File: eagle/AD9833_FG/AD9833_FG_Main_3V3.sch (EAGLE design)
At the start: 12 parts, among them IC1 AD822N

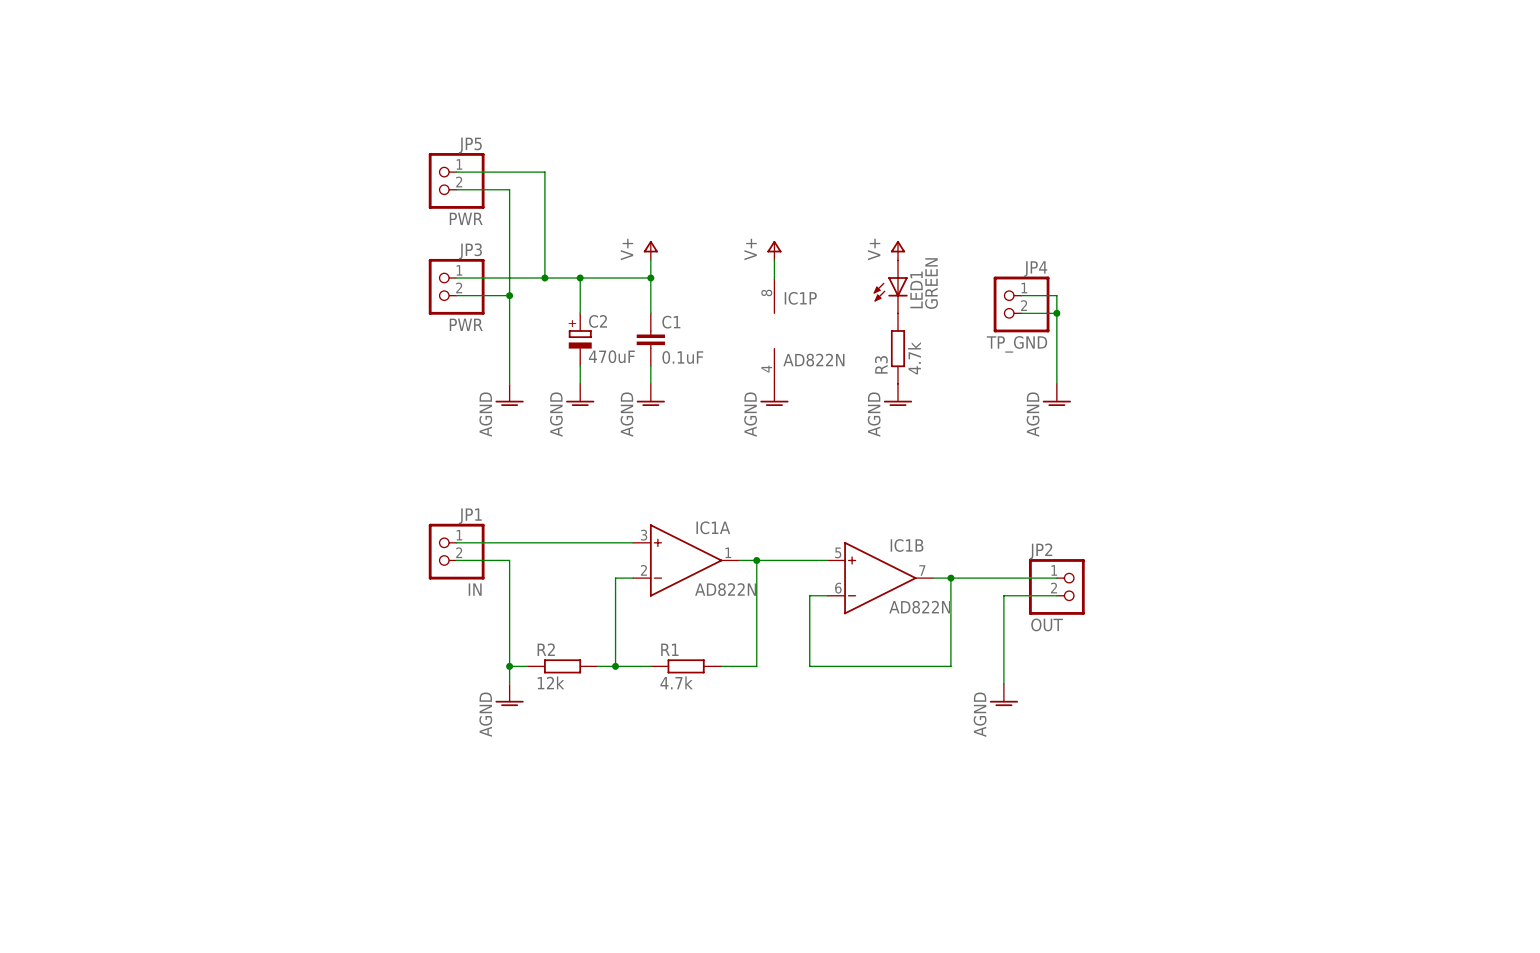
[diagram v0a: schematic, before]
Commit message: 3.3V Version
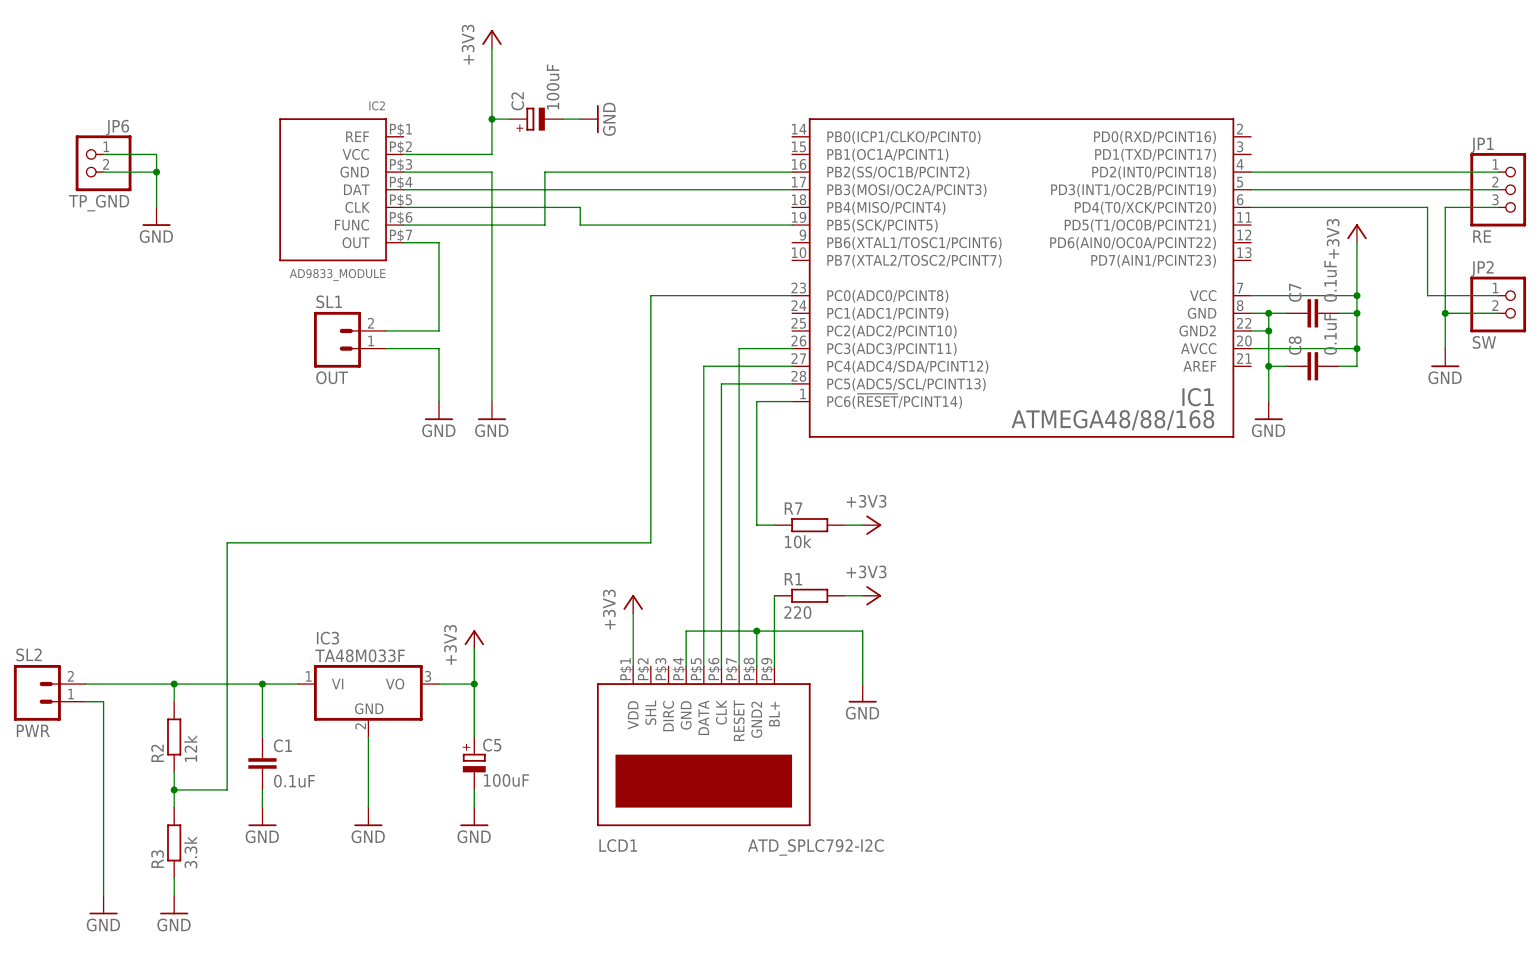
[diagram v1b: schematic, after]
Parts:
- removed JP3, JP5: PWR, pinhead:PINHD-1X2
- removed JP4: TP_GND, pinhead:PINHD-1X2
- removed LED1: GREEN, led:LED3MM
- added C5: 100uF, rcl:CPOL-EUSANYO_C
- added C7, C8: 0.1uF, rcl:C-EU025-024X044
- added IC2: AD9833_MODULE, mylib2:AD9833_MODULE
- added IC3: TA48M033F, mylib2:TA48M033F
- added JP6: TP_GND, pinhead:PINHD-1X2
- added LCD1: ATD_SPLC792-I2C, mylib2:ATD_SPLC792-I2C
- added R7: 10k, rcl:R-EU_0207/7
- added SL1: OUT, con-amp-quick:M02
- added SL2: PWR, con-amp-quick:M02
- C2: value 470uF -> 100uF; device rcl:CPOL-EUE2.5-7 -> rcl:CPOL-EUSANYO_C
- IC1: value AD822N -> ATMEGA48/88/168; device analog-devices:AD822N -> mylib2:ATMEGA48/88/168
- JP1: value IN -> RE; device pinhead:PINHD-1X2 -> pinhead:PINHD-1X3
- JP2: value OUT -> SW
- R1: value 4.7k -> 220
- R3: value 4.7k -> 3.3k
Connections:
- removed net AGND: C1.2, C2.-, IC1P.V-, JP1.2, JP2.2, JP3.2, JP4.1, JP4.2, JP5.2, R2.1, R3.1
- removed net V+: C1.1, C2.+, IC1P.V+, JP3.1, JP5.1, LED1.A
- new net +3V3: C2.+, C5.+, C7.2, C8.2, IC1.AVCC, IC1.VCC, IC2.VCC, IC3.VO, LCD1.VDD, R1.2, R7.2
- new net GND: C1.2, C2.-, C5.-, C7.1, C8.1, IC1.GND, IC1.GND2, IC2.GND, IC3.GND, JP1.3, JP2.2, JP6.1, JP6.2, LCD1.GND, LCD1.GND2, R3.1, SL1.1, SL2.1
- new net N$10: IC1.PD4(T0/XCK/PCINT20), JP2.1
- new net N$14: LCD1.BL+, R1.1
- new net N$15: C1.1, IC3.VI, R2.2, SL2.2
- new net N$16: IC1.PC0(ADC0/PCINT8), R2.1, R3.2
- new net N$18: IC1.PC6(!RESET!/PCINT14), R7.1
- new net N$2: IC1.PB5(SCK/PCINT5), IC2.CLK
- new net N$6: IC2.OUT, SL1.2
- new net N$7: IC1.PC3(ADC3/PCINT11), LCD1.RESET
- new net N$9: IC1.PD3(INT1/OC2B/PCINT19), JP1.2
- net N$1: now also IC1.PB3(MOSI/OC2A/PCINT3), IC2.DAT; no longer IC1A.IN-, R1.1, R2.2
- net N$3: now also IC1.PB2(SS/OC1B/PCINT2), IC2.FUNC; no longer IC1A.IN+, JP1.1
- net N$4: now also IC1.PC5(ADC5/SCL/PCINT13), LCD1.CLK; no longer IC1A.OUT, IC1B.IN+, R1.2
- net N$5: now also IC1.PC4(ADC4/SDA/PCINT12), LCD1.DATA; no longer IC1B.IN-, IC1B.OUT, JP2.1
- net N$8: now also IC1.PD2(INT0/PCINT18), JP1.1; no longer LED1.C, R3.2
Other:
- moved on the sheet: C1, C2, JP2, R1, R2, R3

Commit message: Board Design
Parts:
- added SL3: PWR, con-amp-quick:M02
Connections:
- net GND: now also SL2.2, SL3.1; no longer SL2.1
- net N$15: now also SL2.1, SL3.2; no longer SL2.2
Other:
- moved on the sheet: SL2
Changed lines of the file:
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@@
 <setting verticaltext="up"/>
 </settings>
-<grid distance="0.1" unitdist="inch" unit="inch" style="lines" multiple="1" display="yes" altdistance="0.01" altunitdist="inch" altunit="inch"/>
+<grid distance="0.1" unitdist="inch" unit="inch" style="lines" multiple="1" display="no" altdistance="0.01" altunitdist="inch" altunit="inch"/>
 <layers>
 <layer number="1" name="Top" color="4" fill="1" visible="no" active="no"/>
@@
 <part name="C2" library="rcl" deviceset="CPOL-EU" device="SANYO_C" value="100uF"/>
 <part name="GND4" library="supply1" deviceset="GND" device=""/>
+<part name="SL3" library="con-amp-quick" deviceset="M02" device="" value="PWR"/>
 </parts>
 <sheets>
@@
 <instance part="C8" gate="G$1" x="210.82" y="111.76" rot="R90"/>
 <instance part="SL1" gate="G$1" x="71.12" y="114.3"/>
-<instance part="SL2" gate="G$1" x="27.94" y="63.5"/>
+<instance part="SL2" gate="G$1" x="27.94" y="66.04" rot="MR180"/>
 <instance part="+3V2" gate="G$1" x="91.44" y="73.66"/>
 <instance part="+3V4" gate="G$1" x="93.98" y="160.02"/>
@@
 <instance part="C2" gate="G$1" x="99.06" y="147.32" rot="R90"/>
 <instance part="GND4" gate="1" x="109.22" y="147.32" rot="R90"/>
+<instance part="SL3" gate="G$1" x="27.94" y="48.26"/>
 </instances>
 <busses>
@@
 <segment>
 <pinref part="GND3" gate="1" pin="GND"/>
+<pinref part="JP1" gate="A" pin="3"/>
 <wire x1="231.14" y1="114.3" x2="231.14" y2="119.38" width="0.1524" layer="91"/>
-<pinref part="JP1" gate="A" pin="3"/>
 <wire x1="231.14" y1="119.38" x2="231.14" y2="134.62" width="0.1524" layer="91"/>
 <wire x1="231.14" y1="134.62" x2="238.76" y2="134.62" width="0.1524" layer="91"/>
@@
 </segment>
 <segment>
+<pinref part="GND7" gate="1" pin="GND"/>
+<wire x1="38.1" y1="63.5" x2="38.1" y2="48.26" width="0.1524" layer="91"/>
+<pinref part="SL3" gate="G$1" pin="1"/>
+<wire x1="38.1" y1="48.26" x2="38.1" y2="35.56" width="0.1524" layer="91"/>
+<wire x1="35.56" y1="48.26" x2="38.1" y2="48.26" width="0.1524" layer="91"/>
+<junction x="38.1" y="48.26"/>
+<pinref part="SL2" gate="G$1" pin="2"/>
 <wire x1="35.56" y1="63.5" x2="38.1" y2="63.5" width="0.1524" layer="91"/>
-<pinref part="GND7" gate="1" pin="GND"/>
-<wire x1="38.1" y1="63.5" x2="38.1" y2="35.56" width="0.1524" layer="91"/>
-<pinref part="SL2" gate="G$1" pin="1"/>
 </segment>
 <segment>
@@
 <net name="N$15" class="0">
 <segment>
-<wire x1="35.56" y1="66.04" x2="48.26" y2="66.04" width="0.1524" layer="91"/>
+<wire x1="43.18" y1="66.04" x2="48.26" y2="66.04" width="0.1524" layer="91"/>
 <wire x1="48.26" y1="66.04" x2="60.96" y2="66.04" width="0.1524" layer="91"/>
 <wire x1="60.96" y1="58.42" x2="60.96" y2="66.04" width="0.1524" layer="91"/>
@@
 <wire x1="48.26" y1="63.5" x2="48.26" y2="66.04" width="0.1524" layer="91"/>
 <junction x="48.26" y="66.04"/>
-<pinref part="SL2" gate="G$1" pin="2"/>
 <wire x1="66.04" y1="66.04" x2="60.96" y2="66.04" width="0.1524" layer="91"/>
 <junction x="60.96" y="66.04"/>
 <pinref part="C1" gate="G$1" pin="1"/>
 <pinref part="IC3" gate="G$1" pin="VI"/>
-</segment>
-</net>
+<pinref part="SL3" gate="G$1" pin="2"/>
+<wire x1="35.56" y1="50.8" x2="43.18" y2="50.8" width="0.1524" layer="91"/>
+<wire x1="43.18" y1="50.8" x2="43.18" y2="66.04" width="0.1524" layer="91"/>
+<pinref part="SL2" gate="G$1" pin="1"/>
+<wire x1="35.56" y1="66.04" x2="43.18" y2="66.04" width="0.1524" layer="91"/>
+<junction x="43.18" y="66.04"/>
+</segment>
+</net>

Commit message: Update eagle files
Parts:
- removed R3: 3.3k, rcl:R-EU_0207/7
- removed SL3: PWR, con-amp-quick:M02
- added JP3: TP_3V3, pinhead:PINHD-1X2
- added R4: 100k, pot:TRIM_EU-B25P
- C5: device rcl:CPOL-EUSANYO_C -> rcl:CPOL-EUE2.5-7
- C8: device rcl:C-EU025-024X044 -> rcl:C-EU050-024X044
- R2: value 12k -> 220k
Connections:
- new net N$11: R2.1, R4.E
- net +3V3: now also JP3.1, JP3.2
- net GND: now also R4.A; no longer R3.1, SL3.1
- net N$15: no longer SL3.2
- net N$16: now also R4.S; no longer R2.1, R3.2
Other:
- moved on the sheet: JP6
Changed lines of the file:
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@@
 <setting verticaltext="up"/>
 </settings>
-<grid distance="0.1" unitdist="inch" unit="inch" style="lines" multiple="1" display="no" altdistance="0.01" altunitdist="inch" altunit="inch"/>
+<grid distance="0.1" unitdist="inch" unit="inch" style="lines" multiple="1" display="yes" altdistance="0.01" altunitdist="inch" altunit="inch"/>
 <layers>
 <layer number="1" name="Top" color="4" fill="1" visible="no" active="no"/>
@@
 <part name="GND8" library="supply1" deviceset="GND" device=""/>
 <part name="GND9" library="supply1" deviceset="GND" device=""/>
-<part name="C5" library="rcl" deviceset="CPOL-EU" device="SANYO_C" value="100uF"/>
+<part name="C5" library="rcl" deviceset="CPOL-EU" device="E2.5-7" value="100uF"/>
 <part name="GND11" library="supply1" deviceset="GND" device=""/>
-<part name="R2" library="rcl" deviceset="R-EU_" device="0207/7" value="12k"/>
-<part name="R3" library="rcl" deviceset="R-EU_" device="0207/7" value="3.3k"/>
+<part name="R2" library="rcl" deviceset="R-EU_" device="0207/7" value="220k"/>
 <part name="GND12" library="supply1" deviceset="GND" device=""/>
 <part name="FRAME1" library="frames" deviceset="A4L-LOC" device="" value="Frame"/>
@@
 <part name="GND18" library="supply1" deviceset="GND" device=""/>
 <part name="C7" library="rcl" deviceset="C-EU" device="025-024X044" value="0.1uF"/>
-<part name="C8" library="rcl" deviceset="C-EU" device="025-024X044" value="0.1uF"/>
+<part name="C8" library="rcl" deviceset="C-EU" device="050-024X044" value="0.1uF"/>
 <part name="SL1" library="con-amp-quick" deviceset="M02" device="" value="OUT"/>
 <part name="SL2" library="con-amp-quick" deviceset="M02" device="" value="PWR"/>
@@
 <part name="C2" library="rcl" deviceset="CPOL-EU" device="SANYO_C" value="100uF"/>
 <part name="GND4" library="supply1" deviceset="GND" device=""/>
-<part name="SL3" library="con-amp-quick" deviceset="M02" device="" value="PWR"/>
+<part name="R4" library="pot" deviceset="TRIM_EU-" device="B25P" value="100k"/>
+<part name="JP3" library="pinhead" deviceset="PINHD-1X2" device="" value="TP_3V3"/>
+<part name="+3V3" library="supply1" deviceset="+3V3" device=""/>
 </parts>
 <sheets>
@@
 <instance part="GND11" gate="1" x="91.44" y="45.72"/>
 <instance part="R2" gate="G$1" x="48.26" y="58.42" rot="R90"/>
-<instance part="R3" gate="G$1" x="48.26" y="43.18" rot="R90"/>
 <instance part="GND12" gate="1" x="48.26" y="33.02"/>
 <instance part="FRAME1" gate="G$1" x="0" y="0"/>
-<instance part="JP6" gate="G$1" x="35.56" y="139.7" rot="MR0"/>
-<instance part="GND16" gate="1" x="45.72" y="132.08"/>
+<instance part="JP6" gate="G$1" x="35.56" y="124.46" rot="MR0"/>
+<instance part="GND16" gate="1" x="45.72" y="116.84"/>
 <instance part="R7" gate="G$1" x="139.7" y="88.9"/>
 <instance part="GND18" gate="1" x="205.74" y="104.14"/>
@@
 <instance part="C2" gate="G$1" x="99.06" y="147.32" rot="R90"/>
 <instance part="GND4" gate="1" x="109.22" y="147.32" rot="R90"/>
-<instance part="SL3" gate="G$1" x="27.94" y="48.26"/>
+<instance part="R4" gate="1" x="48.26" y="45.72" smashed="yes">
+<attribute name="NAME" x="42.291" y="41.91" size="1.778" layer="95" rot="R90"/>
+<attribute name="VALUE" x="44.45" y="41.91" size="1.778" layer="96" rot="R90"/>
+</instance>
+<instance part="JP3" gate="G$1" x="35.56" y="142.24" rot="MR0"/>
+<instance part="+3V3" gate="G$1" x="45.72" y="154.94"/>
 </instances>
 <busses>
@@
 <segment>
 <pinref part="GND7" gate="1" pin="GND"/>
-<wire x1="38.1" y1="63.5" x2="38.1" y2="48.26" width="0.1524" layer="91"/>
-<pinref part="SL3" gate="G$1" pin="1"/>
-<wire x1="38.1" y1="48.26" x2="38.1" y2="35.56" width="0.1524" layer="91"/>
-<wire x1="35.56" y1="48.26" x2="38.1" y2="48.26" width="0.1524" layer="91"/>
-<junction x="38.1" y="48.26"/>
+<wire x1="38.1" y1="63.5" x2="38.1" y2="35.56" width="0.1524" layer="91"/>
 <pinref part="SL2" gate="G$1" pin="2"/>
 <wire x1="35.56" y1="63.5" x2="38.1" y2="63.5" width="0.1524" layer="91"/>
@@
 <segment>
 <pinref part="GND12" gate="1" pin="GND"/>
-<pinref part="R3" gate="G$1" pin="1"/>
-<wire x1="48.26" y1="35.56" x2="48.26" y2="38.1" width="0.1524" layer="91"/>
+<wire x1="48.26" y1="35.56" x2="48.26" y2="40.64" width="0.1524" layer="91"/>
+<pinref part="R4" gate="1" pin="A"/>
 </segment>
 <segment>
 <pinref part="JP6" gate="G$1" pin="2"/>
-<wire x1="38.1" y1="139.7" x2="45.72" y2="139.7" width="0.1524" layer="91"/>
-<wire x1="45.72" y1="139.7" x2="45.72" y2="142.24" width="0.1524" layer="91"/>
+<wire x1="38.1" y1="124.46" x2="45.72" y2="124.46" width="0.1524" layer="91"/>
+<wire x1="45.72" y1="124.46" x2="45.72" y2="127" width="0.1524" layer="91"/>
 <pinref part="JP6" gate="G$1" pin="1"/>
-<wire x1="45.72" y1="142.24" x2="38.1" y2="142.24" width="0.1524" layer="91"/>
+<wire x1="45.72" y1="127" x2="38.1" y2="127" width="0.1524" layer="91"/>
 <pinref part="GND16" gate="1" pin="GND"/>
-<wire x1="45.72" y1="139.7" x2="45.72" y2="134.62" width="0.1524" layer="91"/>
-<junction x="45.72" y="139.7"/>
+<wire x1="45.72" y1="124.46" x2="45.72" y2="119.38" width="0.1524" layer="91"/>
+<junction x="45.72" y="124.46"/>
 </segment>
 <segment>
@@
 <pinref part="+3V7" gate="G$1" pin="+3V3"/>
 </segment>
+<segment>
+<pinref part="JP3" gate="G$1" pin="2"/>
+<wire x1="38.1" y1="142.24" x2="45.72" y2="142.24" width="0.1524" layer="91"/>
+<wire x1="45.72" y1="142.24" x2="45.72" y2="144.78" width="0.1524" layer="91"/>
+<pinref part="+3V3" gate="G$1" pin="+3V3"/>
+<pinref part="JP3" gate="G$1" pin="1"/>
+<wire x1="45.72" y1="144.78" x2="45.72" y2="152.4" width="0.1524" layer="91"/>
+<wire x1="38.1" y1="144.78" x2="45.72" y2="144.78" width="0.1524" layer="91"/>
+<junction x="45.72" y="144.78"/>
+</segment>
 </net>
 <net name="N$14" class="0">
@@
 <net name="N$15" class="0">
 <segment>
-<wire x1="43.18" y1="66.04" x2="48.26" y2="66.04" width="0.1524" layer="91"/>
 <wire x1="48.26" y1="66.04" x2="60.96" y2="66.04" width="0.1524" layer="91"/>
 <wire x1="60.96" y1="58.42" x2="60.96" y2="66.04" width="0.1524" layer="91"/>
@@
 <pinref part="C1" gate="G$1" pin="1"/>
 <pinref part="IC3" gate="G$1" pin="VI"/>
-<pinref part="SL3" gate="G$1" pin="2"/>
-<wire x1="35.56" y1="50.8" x2="43.18" y2="50.8" width="0.1524" layer="91"/>
-<wire x1="43.18" y1="50.8" x2="43.18" y2="66.04" width="0.1524" layer="91"/>
 <pinref part="SL2" gate="G$1" pin="1"/>
-<wire x1="35.56" y1="66.04" x2="43.18" y2="66.04" width="0.1524" layer="91"/>
-<junction x="43.18" y="66.04"/>
+<wire x1="35.56" y1="66.04" x2="48.26" y2="66.04" width="0.1524" layer="91"/>
 </segment>
 </net>
@@
 <wire x1="116.84" y1="121.92" x2="137.16" y2="121.92" width="0.1524" layer="91"/>
 <wire x1="116.84" y1="121.92" x2="116.84" y2="86.36" width="0.1524" layer="91"/>
-<wire x1="55.88" y1="50.8" x2="55.88" y2="86.36" width="0.1524" layer="91"/>
+<wire x1="55.88" y1="45.72" x2="55.88" y2="86.36" width="0.1524" layer="91"/>
 <wire x1="116.84" y1="86.36" x2="55.88" y2="86.36" width="0.1524" layer="91"/>
-<pinref part="R2" gate="G$1" pin="1"/>
-<pinref part="R3" gate="G$1" pin="2"/>
-<wire x1="48.26" y1="48.26" x2="48.26" y2="50.8" width="0.1524" layer="91"/>
-<wire x1="48.26" y1="50.8" x2="48.26" y2="53.34" width="0.1524" layer="91"/>
-<wire x1="55.88" y1="50.8" x2="48.26" y2="50.8" width="0.1524" layer="91"/>
-<junction x="48.26" y="50.8"/>
+<pinref part="R4" gate="1" pin="S"/>
+<wire x1="53.34" y1="45.72" x2="55.88" y2="45.72" width="0.1524" layer="91"/>
 </segment>
 </net>
@@
 </segment>
 </net>
+<net name="N$11" class="0">
+<segment>
+<pinref part="R2" gate="G$1" pin="1"/>
+<pinref part="R4" gate="1" pin="E"/>
+<wire x1="48.26" y1="50.8" x2="48.26" y2="53.34" width="0.1524" layer="91"/>
+</segment>
+</net>

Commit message: Update
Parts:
- IC1: value ATMEGA48/88/168 -> ATMEGA328P
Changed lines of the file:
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@@
 <part name="JP1" library="pinhead" deviceset="PINHD-1X3" device="" value="RE"/>
 <part name="JP2" library="pinhead" deviceset="PINHD-1X2" device="" value="SW"/>
-<part name="IC1" library="mylib2" deviceset="ATMEGA48/88/168" device=""/>
+<part name="IC1" library="mylib2" deviceset="ATMEGA48/88/168" device="" value="ATMEGA328P"/>
 <part name="IC2" library="mylib2" deviceset="AD9833_MODULE" device=""/>
 <part name="GND1" library="supply1" deviceset="GND" device=""/>
